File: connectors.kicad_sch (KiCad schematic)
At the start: 2 parts, among them J2 Conn_01x02, J3 Conn_01x02

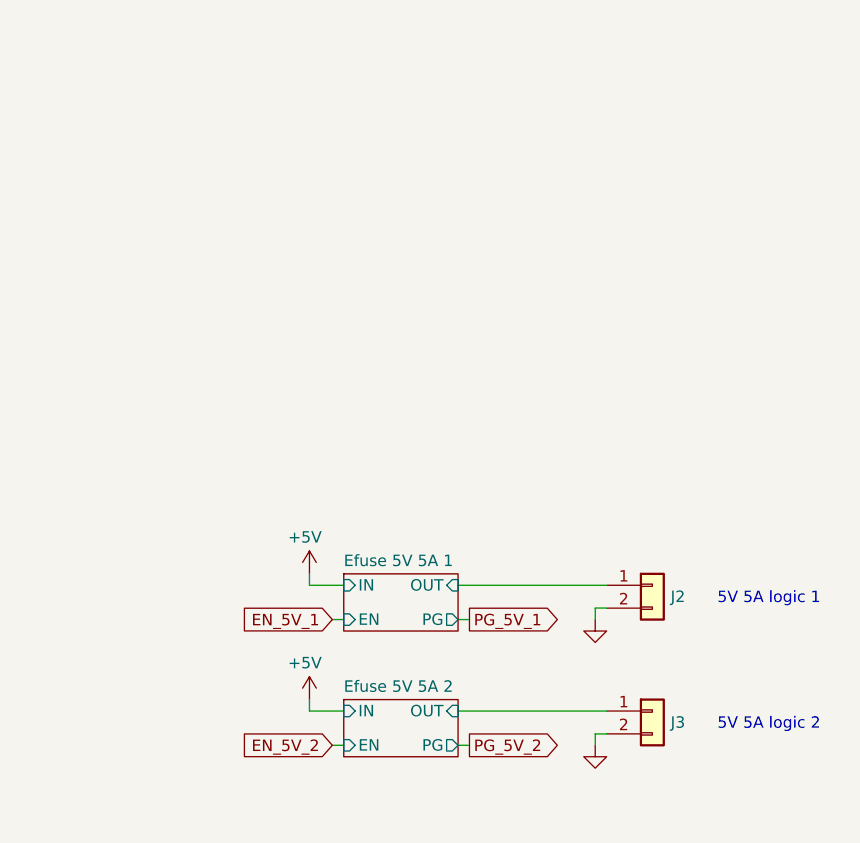
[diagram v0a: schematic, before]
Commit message: schem: add 2 12V 5A rails
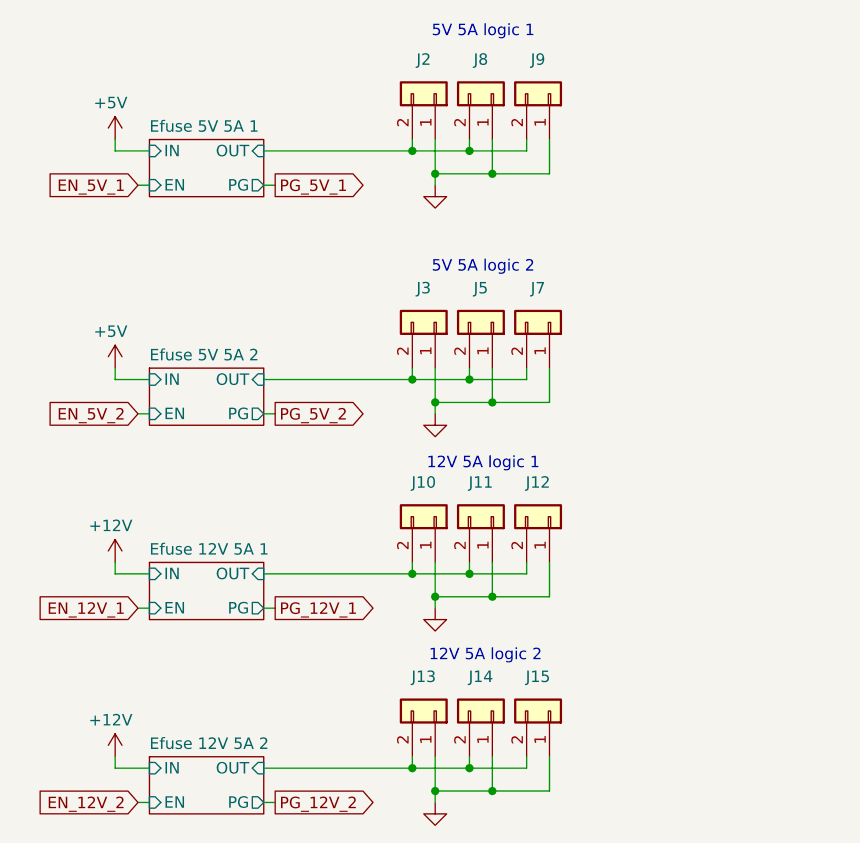
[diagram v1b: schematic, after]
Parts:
- added J10, J11, J12, J13, J14, J15, J5, J7, J8, J9: Conn_01x02, Connector_JST:JST_XH_B2B-XH-A_1x02_P2.50mm_Vertical, symbol Connector_Generic:Conn_01x02
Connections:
- net Efuse 5V 5A 1/OUT: now also J2.2 (Pin_2), J8.2 (Pin_2), J9.2 (Pin_2); no longer J2.1 (Pin_1)
- net Efuse 5V 5A 2/OUT: now also J3.2 (Pin_2), J5.2 (Pin_2), J7.2 (Pin_2); no longer J3.1 (Pin_1)
- net GND: now also J2.1 (Pin_1), J3.1 (Pin_1), J10.1 (Pin_1), J11.1 (Pin_1), J12.1 (Pin_1), J13.1 (Pin_1), J14.1 (Pin_1), J15.1 (Pin_1), J5.1 (Pin_1), J7.1 (Pin_1), J8.1 (Pin_1), J9.1 (Pin_1); no longer J2.2 (Pin_2), J3.2 (Pin_2)
- new net Efuse 12V 5A 1/OUT: J10.2 (Pin_2), J11.2 (Pin_2), J12.2 (Pin_2)
- new net Efuse 12V 5A 2/OUT: J13.2 (Pin_2), J14.2 (Pin_2), J15.2 (Pin_2)
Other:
- added sheet Efuse 12V 5A 1 (efuse-12-5.kicad_sch)
- added sheet Efuse 12V 5A 2 (efuse-12-5.kicad_sch)
- note added: "12V 5A logic 1"
- note added: "12V 5A logic 2"
- moved on the sheet: J2

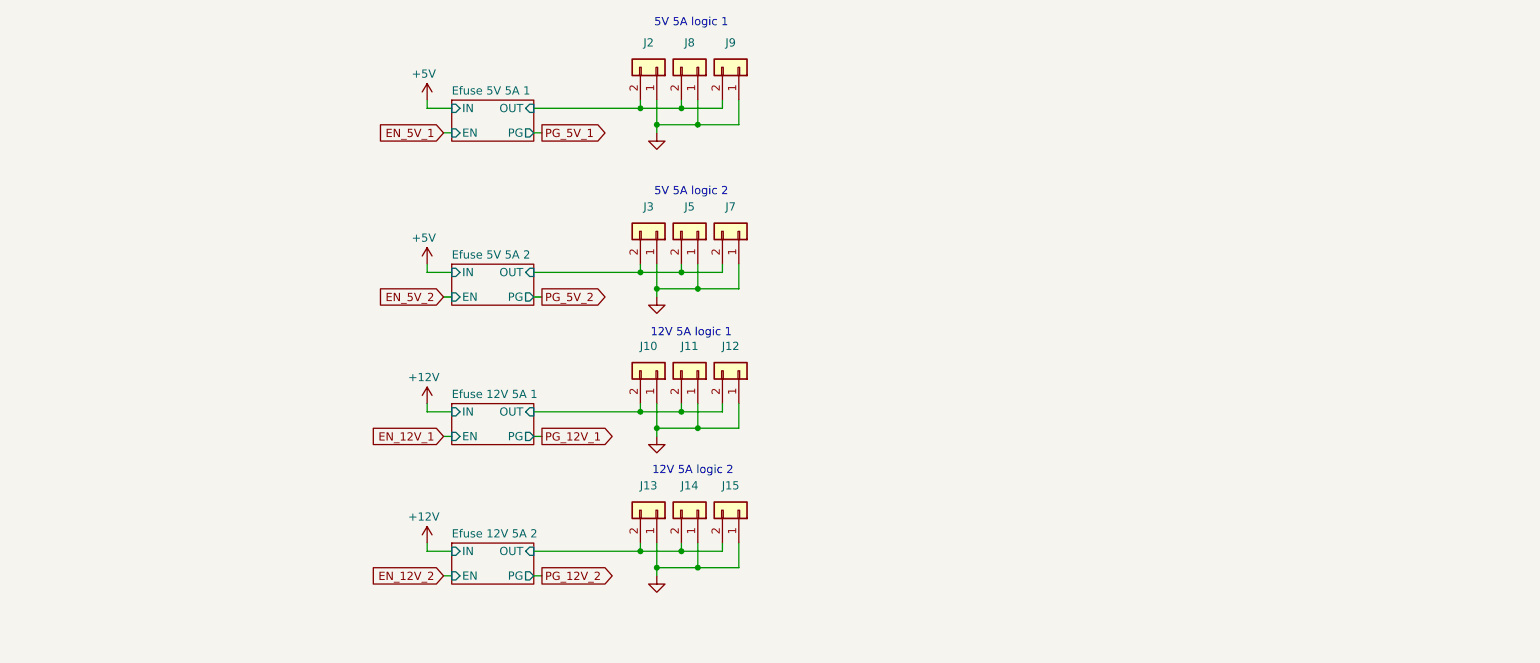
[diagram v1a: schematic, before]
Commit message: schem: add ILM pins and 12V 10A rail
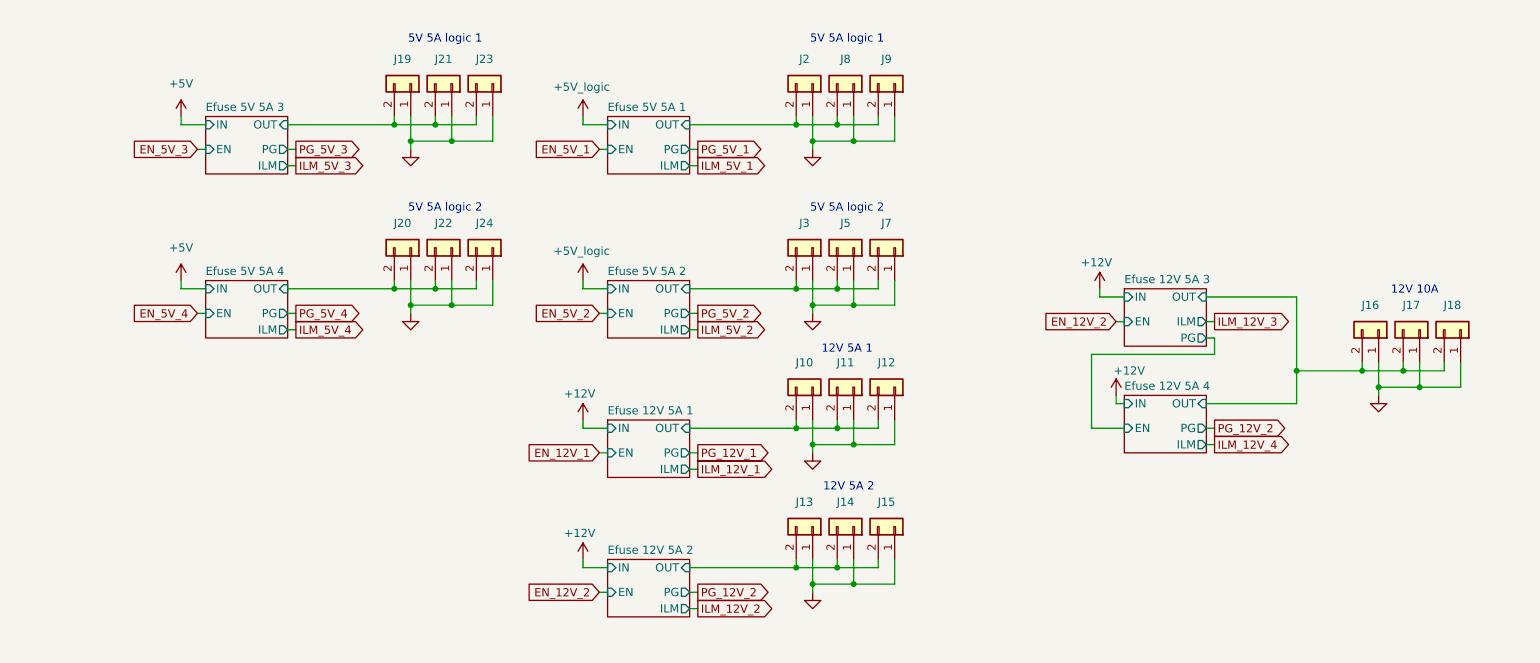
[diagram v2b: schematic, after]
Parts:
- added J16, J17, J18, J19, J20, J21, J22, J23, J24: Conn_01x02, Connector_JST:JST_XH_B2B-XH-A_1x02_P2.50mm_Vertical, symbol Connector_Generic:Conn_01x02
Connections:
- net GND: now also J16.1 (Pin_1), J17.1 (Pin_1), J18.1 (Pin_1), J19.1 (Pin_1), J20.1 (Pin_1), J21.1 (Pin_1), J22.1 (Pin_1), J23.1 (Pin_1), J24.1 (Pin_1)
- new net Efuse 12V 5A 3/OUT: J16.2 (Pin_2), J17.2 (Pin_2), J18.2 (Pin_2)
- new net Efuse 5V 5A 3/OUT: J19.2 (Pin_2), J21.2 (Pin_2), J23.2 (Pin_2)
- new net Efuse 5V 5A 4/OUT: J20.2 (Pin_2), J22.2 (Pin_2), J24.2 (Pin_2)
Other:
- added sheet Efuse 12V 5A 3 (efuse-12-5.kicad_sch)
- added sheet Efuse 12V 5A 4 (efuse-12-5.kicad_sch)
- added sheet Efuse 5V 5A 3 (efuse-5-5.kicad_sch)
- added sheet Efuse 5V 5A 4 (efuse-5-5.kicad_sch)
- sheet Efuse 12V 5A 1 ports: added ILM; removed none
- sheet Efuse 12V 5A 2 ports: added ILM; removed none
- sheet Efuse 5V 5A 1 ports: added ILM; removed none
- sheet Efuse 5V 5A 2 ports: added ILM; removed none
- note added: "12V 10A"
- note added: "12V 5A 1"
- note added: "12V 5A 2"
- note removed: "12V 5A logic 1"
- note removed: "12V 5A logic 2"
- moved on the sheet: J10, J11, J12, J13, J14, J15, J2, J3, J5, J7, J8, J9

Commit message: schem: reorganize connectors
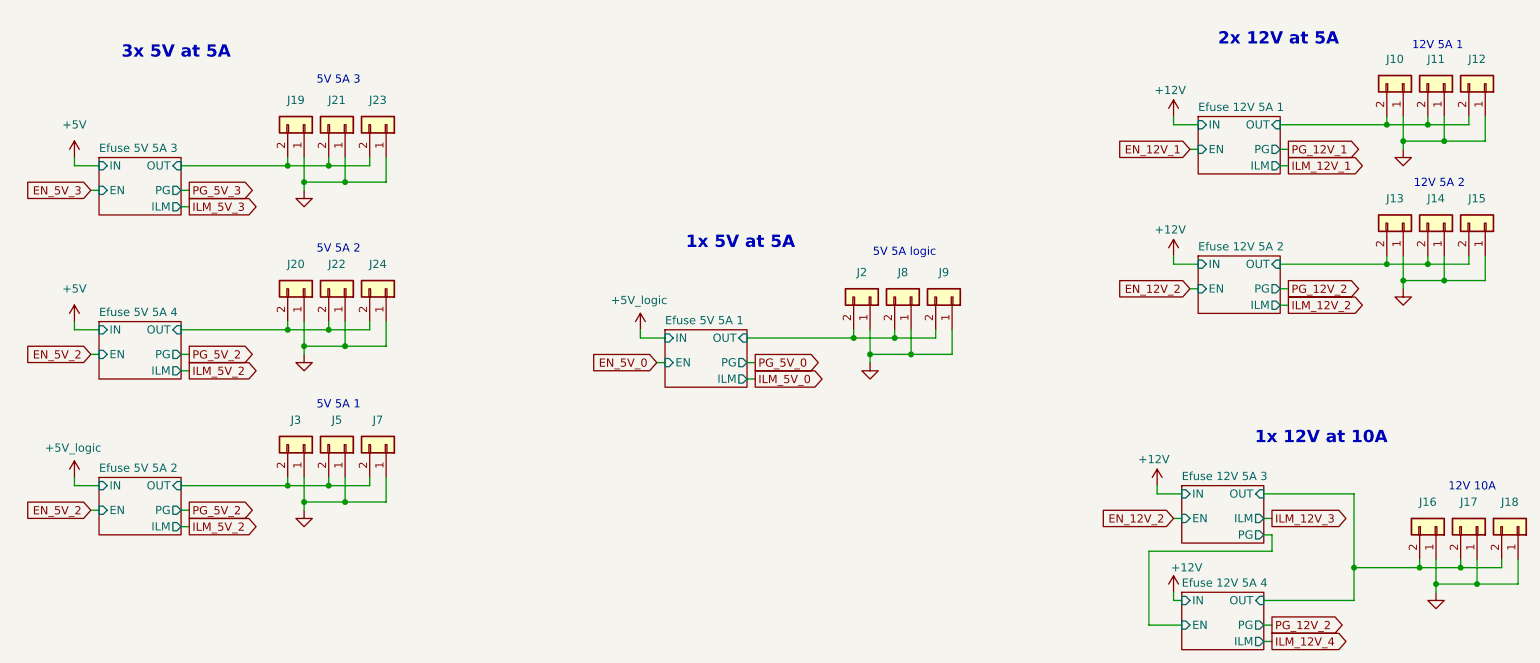
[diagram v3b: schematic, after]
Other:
- note added: "1x 12V at 10A"
- note added: "1x 5V at 5A"
- note added: "2x 12V at 5A"
- note added: "3x 5V at 5A"
- note added: "5V 5A 1"
- note added: "5V 5A 2"
- note added: "5V 5A 3"
- note added: "5V 5A logic"
- note removed: "5V 5A logic 1"
- note removed: "5V 5A logic 2"
- moved on the sheet: J10, J11, J12, J13, J14, J15, J16, J17, J18, J19, J2, J20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
